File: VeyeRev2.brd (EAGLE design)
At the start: 35.6 x 36.1 mm, 35 parts, among them IC1 LP2985AIM5-5.0, SW1 RESET, U1 ATMEGA328P-MU, X2 16MHz

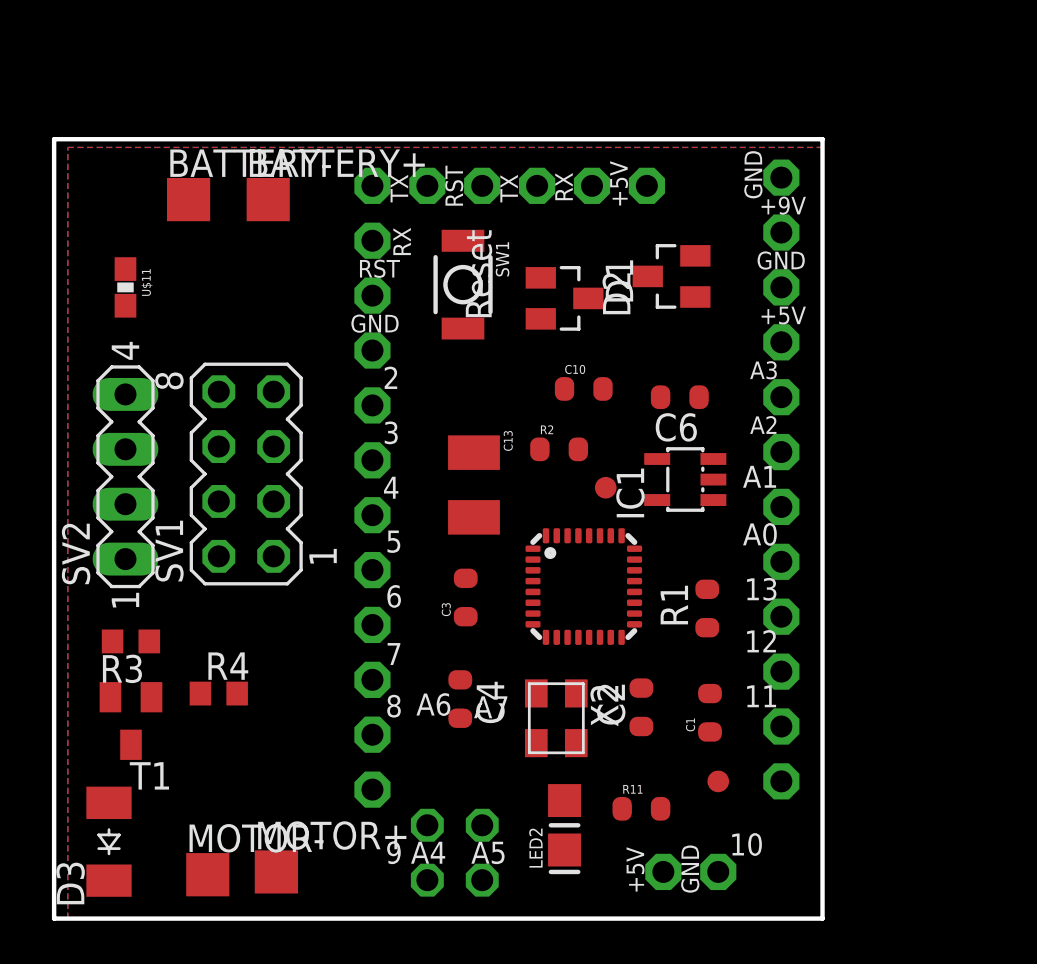
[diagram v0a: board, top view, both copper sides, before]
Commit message: final revisions, smaller board
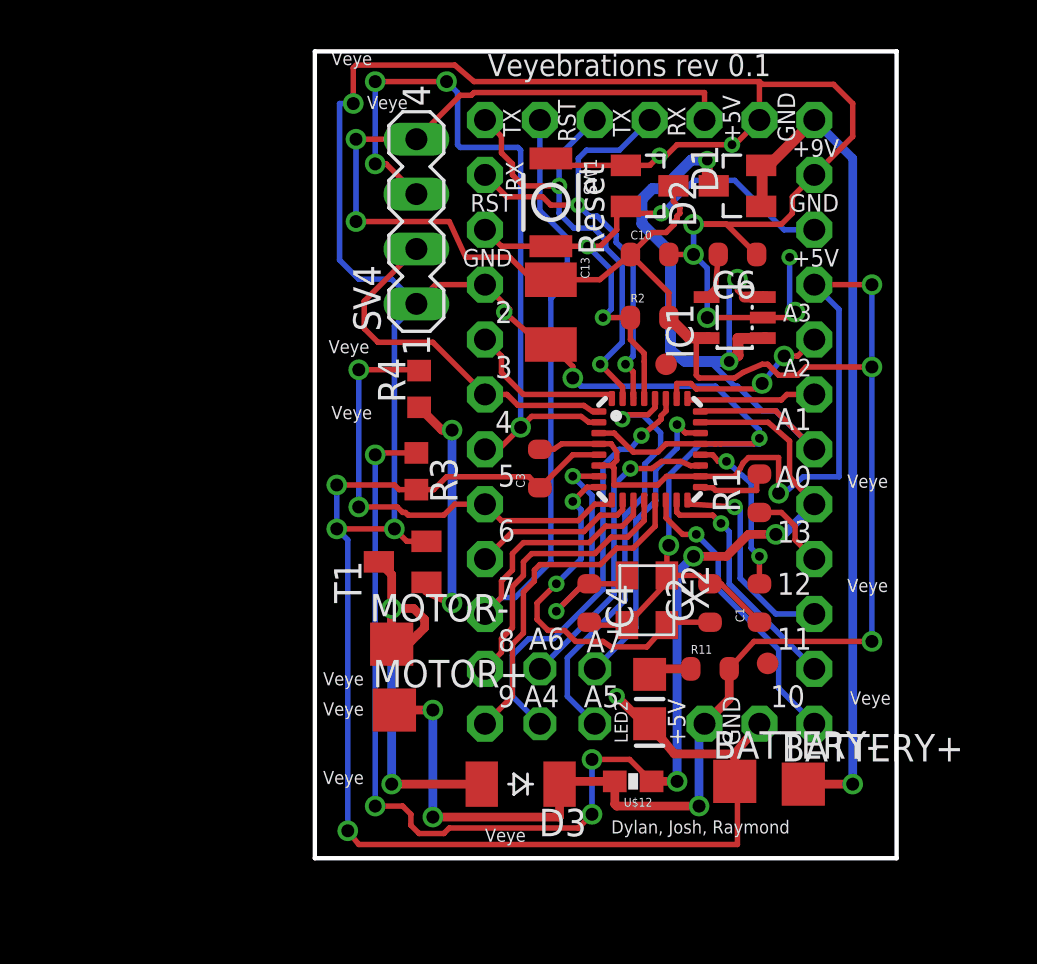
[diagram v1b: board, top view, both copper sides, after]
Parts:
- removed SV1: (no value), con-lstb:MA04-2
- removed SV2: (no value), con-lstb:MA04-1
- removed U$11: NTHS0603N02N1002JE, Veye:0603-RES
- added SV4: (no value), con-lstb:MA04-1
- added U$12: NTHS0603N02N1002JE, Veye:0603-RES
- moved BATTERY- 36.9 mm to (31.6, 6.48)
- moved BATTERY+ 36.7 mm to (34.8, 6.35)
- moved D3 19.2 mm to (21.7, 6.35), turned to 180 degrees
- moved R4 16.9 mm to (17.0, 24.6), turned to 90 degrees
- moved R3 15.4 mm to (16.9, 20.8), turned to 270 degrees
- moved T1 14.6 mm to (16.3, 16.6), turned to 90 degrees
- moved MOTOR- 13.6 mm to (15.7, 12.8)
- moved MOTOR+ 9.27 mm to (15.9, 9.78)
- moved J3 8.92 mm to (23.9, 10.4)
- moved C13 8.76 mm to (23.1, 28.2)
- moved IC1 7.83 mm to (31.6, 27.9)
- moved C4 7.44 mm to (24.9, 14.7)
- moved R2 7.40 mm to (27.7, 27.9)
- moved R11 7.21 mm to (30.5, 11.7)
- moved C6 7.12 mm to (31.8, 30.9)
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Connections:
- removed net ADC1: J2.7
- removed net N$10: SV1.6
- removed net N$11: SV1.4
- removed net N$8: SV1.1
- removed net N$9: SV1.8
- removed net VCC3.3: SV1.2
- net +5V: now also D3.C, SV4.4, U$12.2; no longer SV2.4, U$11.2
- net +VID: now also J2.7
- net ADC0: now also R3.1, U$12.1; no longer U$11.1
- net GND: now also SV4.1; no longer SV1.7, SV2.1
- net IO3: now also SV4.2; no longer SV2.2
- net IO4: now also SV4.3; no longer SV2.3
- net IO7: no longer SV1.5
- net IO8: no longer SV1.3
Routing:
- net GND: track 0.00 -> 205.2 mm, vias 0 -> 17
- net +5V: track 0.00 -> 141.5 mm, vias 0 -> 9
- net ADC0: track 0.00 -> 61.4 mm, vias 0 -> 7
- net VCC: track 0.00 -> 39.8 mm, vias 0 -> 1
- net +VID: track 0.00 -> 38.2 mm, vias 0 -> 3
- net IO7: track 0.00 -> 35.7 mm
- net IO4: track 0.00 -> 34.6 mm, vias 0 -> 4
- net RESET: track 0.00 -> 28.1 mm, vias 0 -> 3
- net IO5: track 0.00 -> 22.0 mm, vias 0 -> 2
- net RX: track 0.00 -> 21.6 mm, vias 0 -> 2
- net TX: track 0.00 -> 21.6 mm, vias 0 -> 2
- net N$13: track 0.00 -> 20.3 mm, vias 0 -> 2
- net ADC5: track 0.00 -> 20.1 mm, vias 0 -> 1
- net ADC4: track 0.00 -> 19.5 mm, vias 0 -> 1
- net N$2: track 0.00 -> 17.4 mm, vias 0 -> 2
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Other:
- board size 35.6 x 36.1 mm -> 26.9 x 37.3 mm
- board text added: "Arduino Wee v1.3"
- board text added: "Dylan, Josh, Raymond"
- board text added: "Tent Vias!"
- board text added: "Veye"
- board text added: "Veyebrations rev 0.1"
